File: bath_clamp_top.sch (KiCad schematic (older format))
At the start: 77 parts, among them J1 105-1103-001, J2 105-1103-001, J3 105-1103-001, J4 HDMI_A, K1 1462042-8, K2 1462042-8, Q1 MBT3904DW1T1G, Q3 MBT3904DW1T1G, Q4 MBT3904DW1T1G, U1 OPA828, U12 TCA9555DBR, U13 TCA9555DBR, U19 TMUX6136PWR, U2 ADG1208, U25 OPA2156xD, U3 G6L-1F-TR-DC5, U4 G6L-1F-TR-DC5, U5 G6L-1F-TR-DC5, U8 OPA2156xD

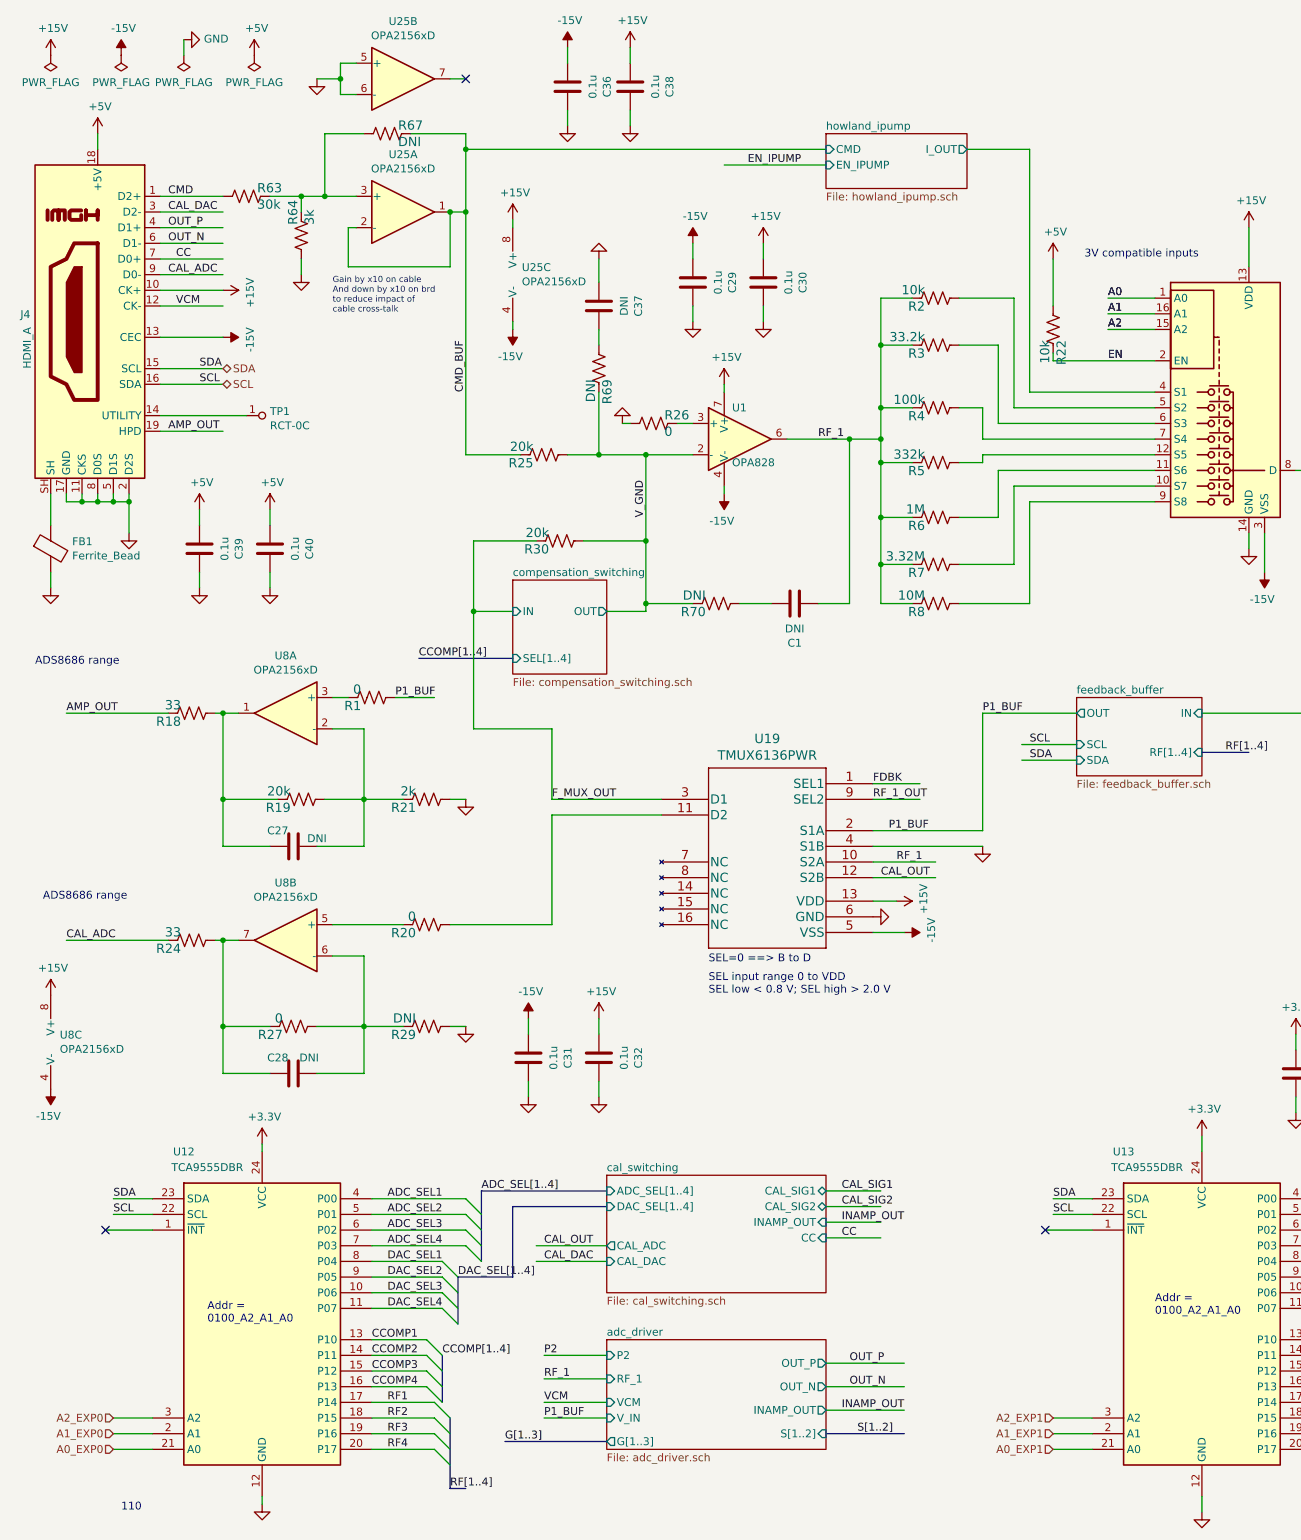
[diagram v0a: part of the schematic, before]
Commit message: added many alternate manufacturing part numbers
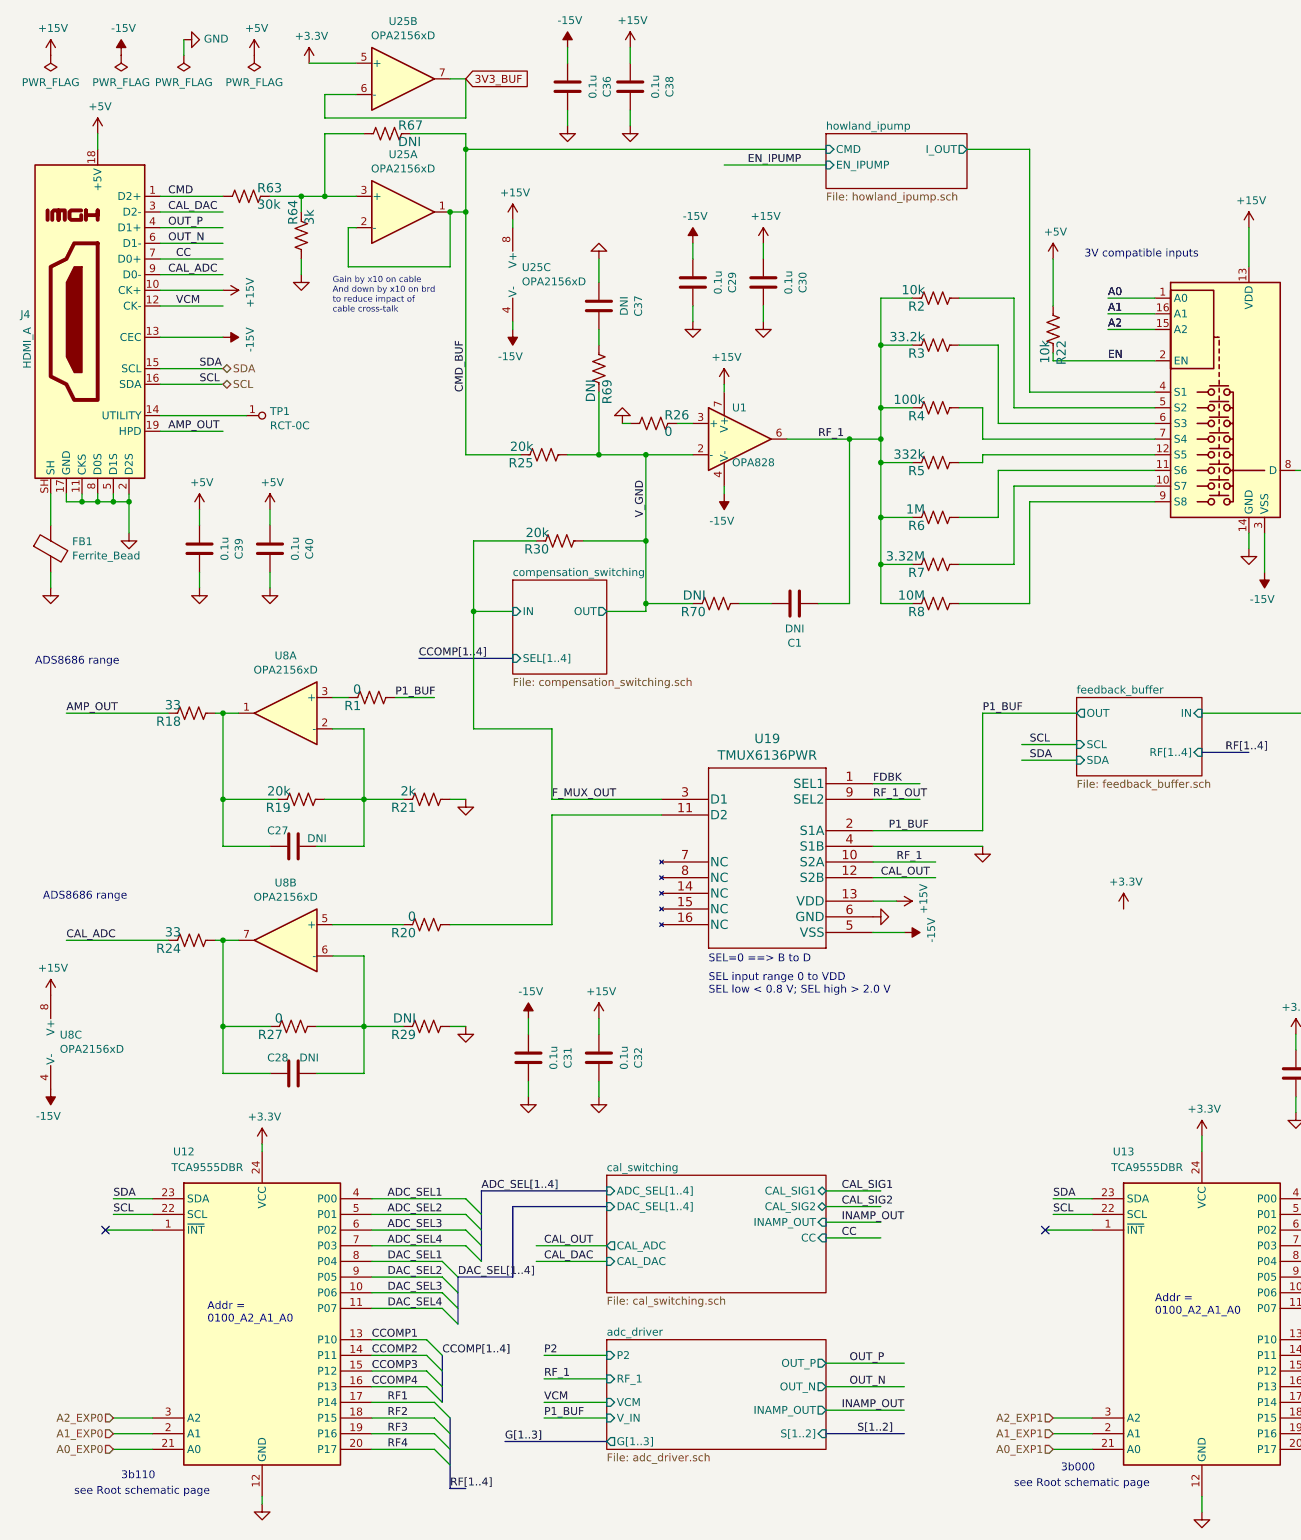
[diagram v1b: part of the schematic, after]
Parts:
- U1: Alternate Manf# (none) -> OPA1641AIDR; Alternate2 Manf# (none) -> OPA1655DR; Alternate3 Manf# (none) -> AD820BRZ; Alternate4 Manf# (none) -> ADA4625-1ARDZ-R7
- U2: Manf# ADG1208YCPZ-REEL7 -> ADG1208YRUZ-REEL7
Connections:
- net labels added: 3V3_BUF
- no-connect marks 5 -> 4
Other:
- note added: "3b000"
- note added: "3b110"
- note added: "see Root schematic page"
- note removed: "110"
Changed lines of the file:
@@
 F 2 "Package_SO:TSSOP-16_4.4x5mm_P0.65mm" H 7450 2050 50  0001 L CNN
 F 3 "https://www.analog.com/media/en/technical-documentation/data-sheets/ADG1208_1209.pdf" H 8210 3000 50  0001 C CNN
-F 4 "ADG1208YCPZ-REEL7" H 8744 3196 50  0001 C CNN "Manf#"
+F 4 "ADG1208YRUZ-REEL7" H 8744 3196 50  0001 C CNN "Manf#"
 	1    8200 3000
 	1    0    0    -1
@@
 F 3 "http://www.ti.com/lit/ds/symlink/opa828.pdf" H 5300 3350 50  0001 C CNN
 F 4 "OPA828ID" H 5150 3200 50  0001 C CNN "Manf#"
+F 5 "OPA1641AIDR" H 5150 3200 50  0001 C CNN "Alternate Manf#"
+F 6 "OPA1655DR" H 5150 3200 50  0001 C CNN "Alternate2 Manf#"
+F 7 "AD820BRZ" H 5150 3200 50  0001 C CNN "Alternate3 Manf#"
+F 8 "ADA4625-1ARDZ-R7" H 5150 3200 50  0001 C CNN "Alternate4 Manf#"
 	1    5150 3200
 	1    0    0    -1
@@
 	3400 1350 5700 1350
 Wire Wire Line
-	2600 800  2700 800
-$Comp
-L power:GND #PWR0174
-U 1 1 6147189F
-P 2450 900
-AR Path="/6032F251/6147189F" Ref="#PWR0174"  Part="1"
-AR Path="/6032F251/608FDC40/6147189F" Ref="#PWR?"  Part="1"
-F 0 "#PWR0174" H 2450 650 50  0001 C CNN
-F 1 "GND" V 2455 772 50  0001 R CNN
-F 2 "" H 2450 900 50  0001 C CNN
-F 3 "" H 2450 900 50  0001 C CNN
-	1    2450 900
-	1    0    0    -1
-$EndComp
-Wire Wire Line
-	2600 1000 2700 1000
-Wire Wire Line
 	3300 900  3400 900
 $Comp
@@
 Text Notes 2550 2400 0    39   ~ 0
 Gain by x10 on cable\nAnd down by x10 on brd\nto reduce impact of \ncable cross-talk
-NoConn ~ 3400 900
 $Comp
 L covg-kicad:G6L-1F-TR-DC5 U3
@@
 Wire Wire Line
 	4550 4250 4550 4300
-Wire Wire Line
-	2600 800  2600 900
-Wire Wire Line
-	2450 900  2600 900
-Connection ~ 2600 900
-Wire Wire Line
-	2600 900  2600 1000
 Text Label 10900 3400 0    50   ~ 0
 P2_OUT
@@
 Wire Wire Line
 	7150 9450 7400 9450
-Text Notes 1200 10050 0    50   ~ 0
-110
 Text HLabel 1150 9650 0    50   Input ~ 0
 A0_EXP0
@@
 	1    0    0    -1
 $EndComp
+Wire Wire Line
+	2500 1000 2500 1150
+Wire Wire Line
+	2500 1150 3400 1150
+Wire Wire Line
+	3400 1150 3400 900
+Wire Wire Line
+	2500 1000 2700 1000
+Wire Wire Line
+	2400 800  2700 800
+$Comp
+L power:+3.3V #PWR?
+U 1 1 625051DB
+P 2400 800
+F 0 "#PWR?" H 2400 650 50  0001 C CNN
+F 1 "+3.3V" H 2415 973 50  0000 C CNN
+F 2 "" H 2400 800 50  0001 C CNN
+F 3 "" H 2400 800 50  0001 C CNN
+	1    2400 800
+	1    0    0    -1
+$EndComp
+Text GLabel 3400 900  2    50   Input ~ 0
+3V3_BUF
 Wire Bus Line
 	9200 9450 9200 9750
@@
 Wire Bus Line
 	3500 8000 3500 8450
+Text Notes 1200 9850 0    50   ~ 0
+3b110
+Text Notes 7200 9800 0    50   ~ 0
+3b000
+Text Notes 900  9950 0    50   ~ 0
+see Root schematic page
+Text Notes 6900 9900 0    50   ~ 0
+see Root schematic page
+$Comp
+L power:+3.3V #PWR?
+U 1 1 6263CFF6
+P 7600 6200
+F 0 "#PWR?" H 7600 6050 50  0001 C CNN
+F 1 "+3.3V" H 7615 6373 50  0000 C CNN
+F 2 "" H 7600 6200 50  0001 C CNN
+F 3 "" H 7600 6200 50  0001 C CNN
+	1    7600 6200
+	1    0    0    -1
+$EndComp
 $EndSCHEMATC

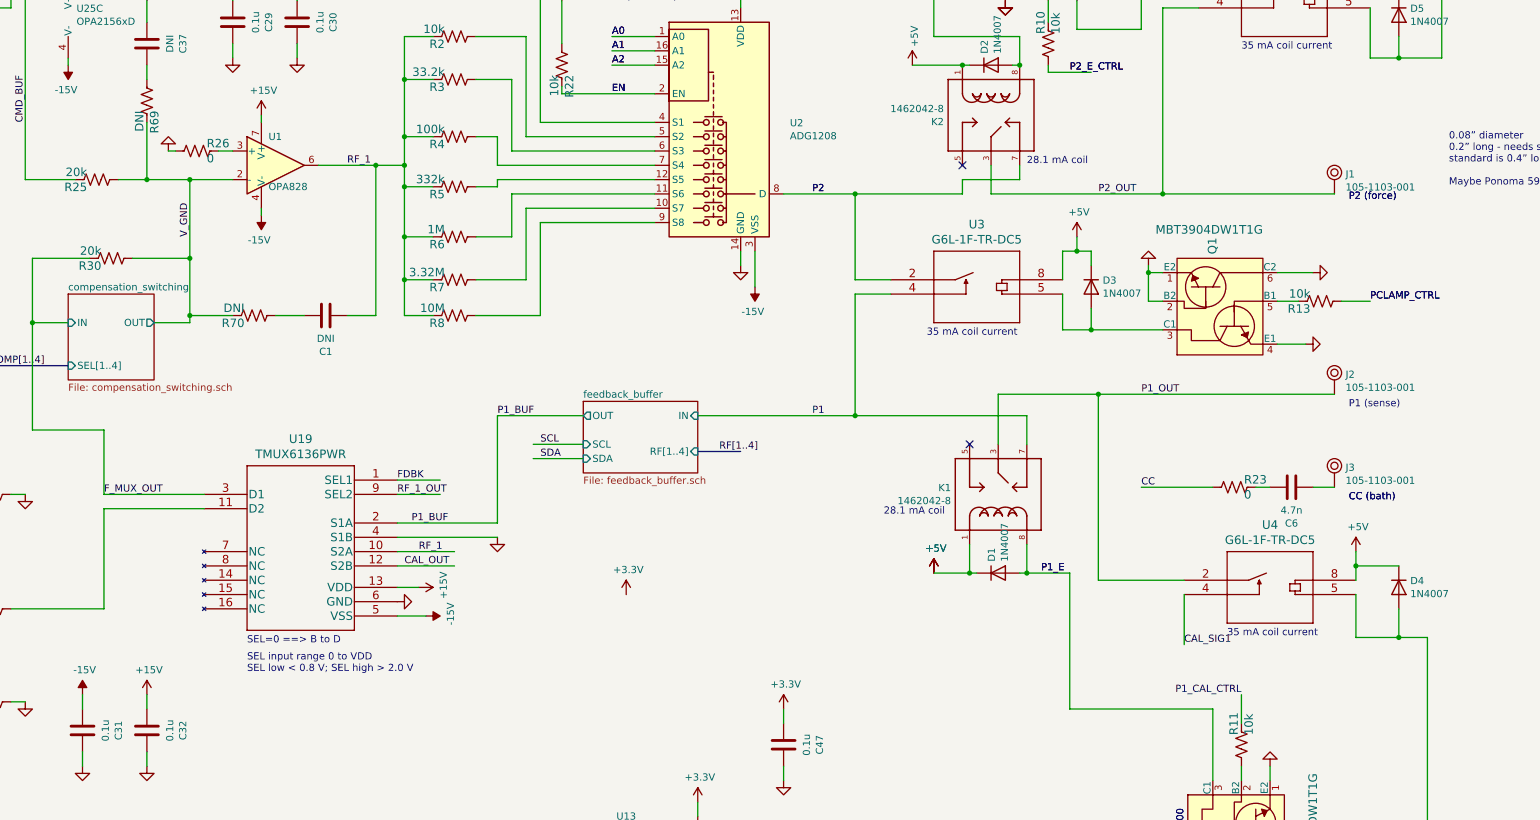
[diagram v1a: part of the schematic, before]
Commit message: updates to schematic for alternate part #s
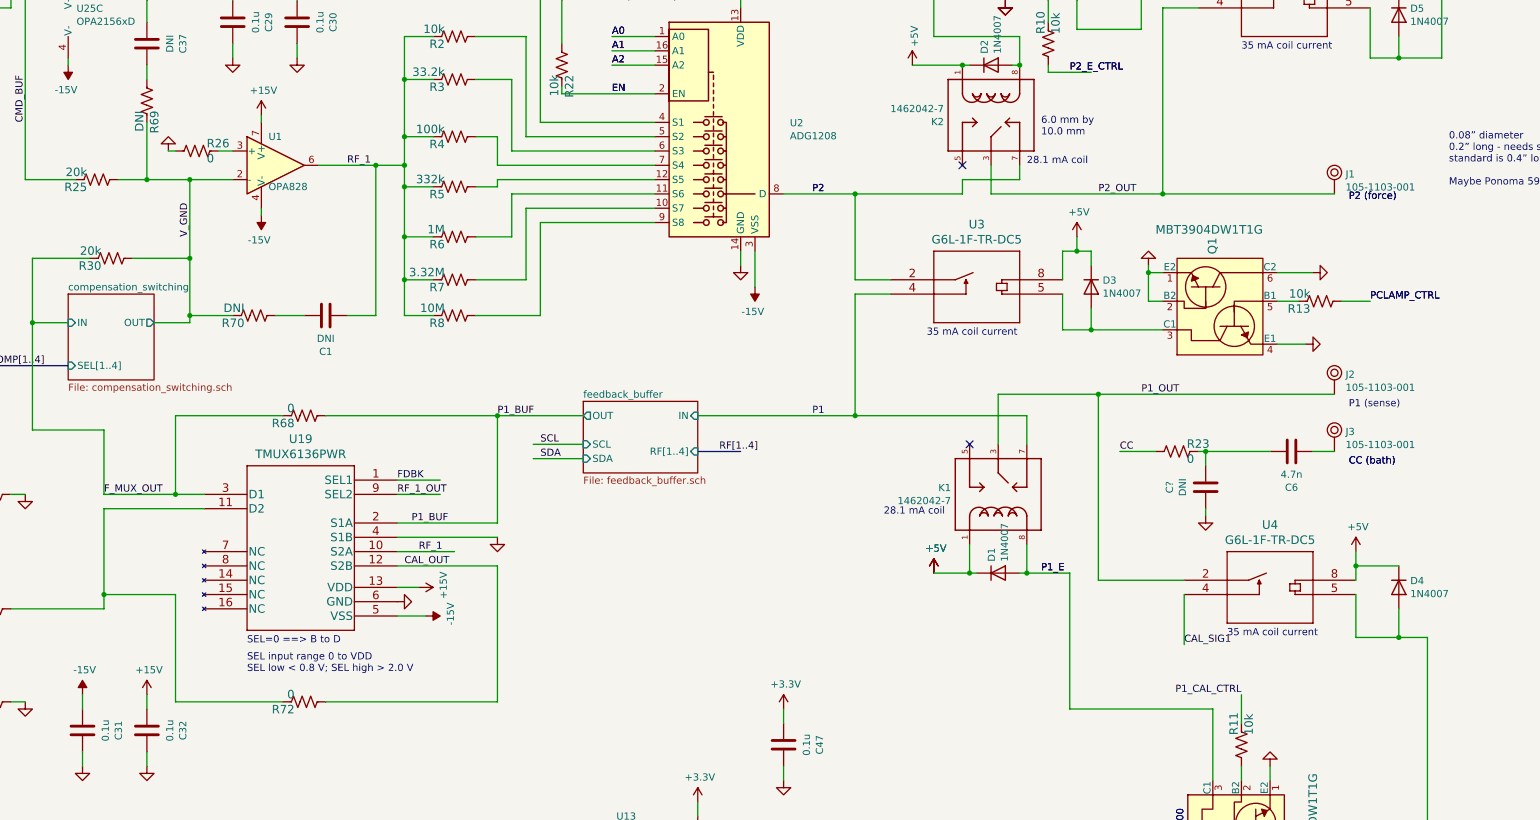
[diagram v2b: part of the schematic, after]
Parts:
- added C?: DNI, Capacitor_SMD:C_0603_1608Metric, symbol Device:C
- added R68, R72: 0, Resistor_SMD:R_0603_1608Metric, symbol Device:R_US
- C27, C28: Manf# (none) -> CC0603FRNPO0BN680
- K1, K2: value 1462042-8 -> 1462042-7; footprint covg-kicad:RELAY_1462042-8 -> covg-kicad:Relay_SPDT_TE_1462042-7; Alternate Manf# (footprint diff) (none) -> 1462042-8; Manf# 1462042-8 -> 1462042-7; PARTREV 917 -> (none); STANDARD Manufacturer recommendation -> (none)
- Q3: MPN MBT3904DW1T1G -> (none)
- R19: Manf# (none) -> RC0603FR-0720KL
- R67: Manf# (none) -> RC0603FR-070RL
- U12, U13: Alternate Manf# (none) -> TCA9555DBT
- U2: Alternate Manf# (none) -> ADG1208YRUZ-REEL7; Manf# ADG1208YRUZ-REEL7 -> MUX36S08IPWR
- U25, U8: Alternate Manf# (none) -> OPA1656ID; Alternate2 Manf# (none) -> OPA1688ID
- U3, U4, U5: Alternate Manf# (none) -> G6L-1F-DC4.5
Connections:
- wire segments 360 -> 373
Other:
- note added: "6.0 mm by \n10.0 mm"
- moved on the sheet: C6, J3, R23
